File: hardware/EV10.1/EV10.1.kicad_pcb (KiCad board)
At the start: 4 copper layers, 72.7 x 89.4 mm, 122 parts, among them J1 Conn_01x02_Socket, J10 Conn_01x08_Socket, J11 Conn_01x06_Female, J13 Conn_01x04_Female, J2 Conn_01x02_Female, J5 Conn_01x02_Socket, J7 Conn_01x04_Female, J8 Conn_01x06_Female, SW4 SW_Push, SW5 SW_Push, U1 STM32F405RGTx, U11 ESP32-S3-WROOM-1-N8R2, U13 BM14B(0.8)-24DS-0.4V(53), U2 BQ21040DBVR, U3 CH340C, U5 STM32F030C8Tx, U6 WM8960CGEFL/RV, U7 TPS63060, Y1 Crystal_GND24

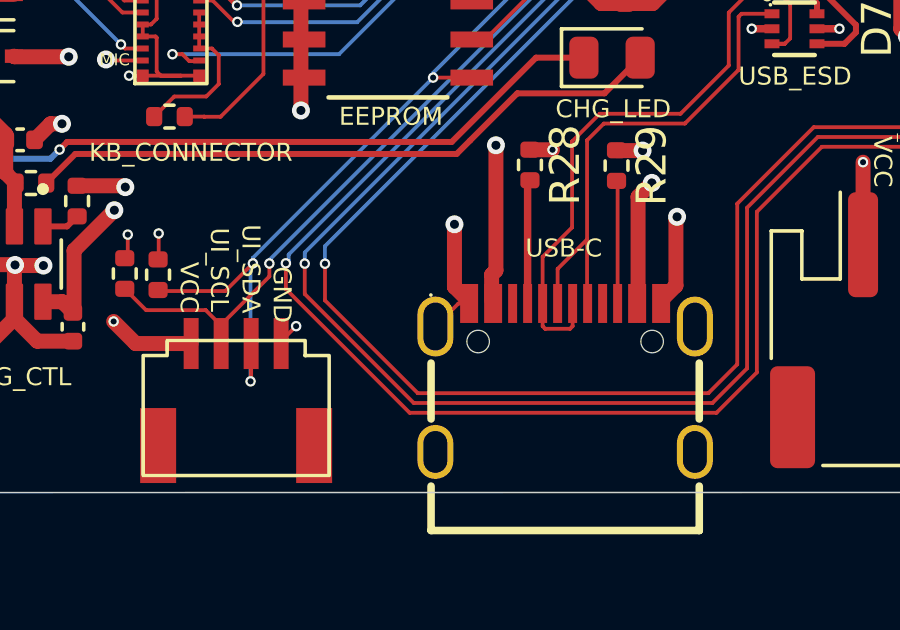
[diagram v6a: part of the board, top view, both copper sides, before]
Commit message: Fixed mistake that grounded the usb-c shield
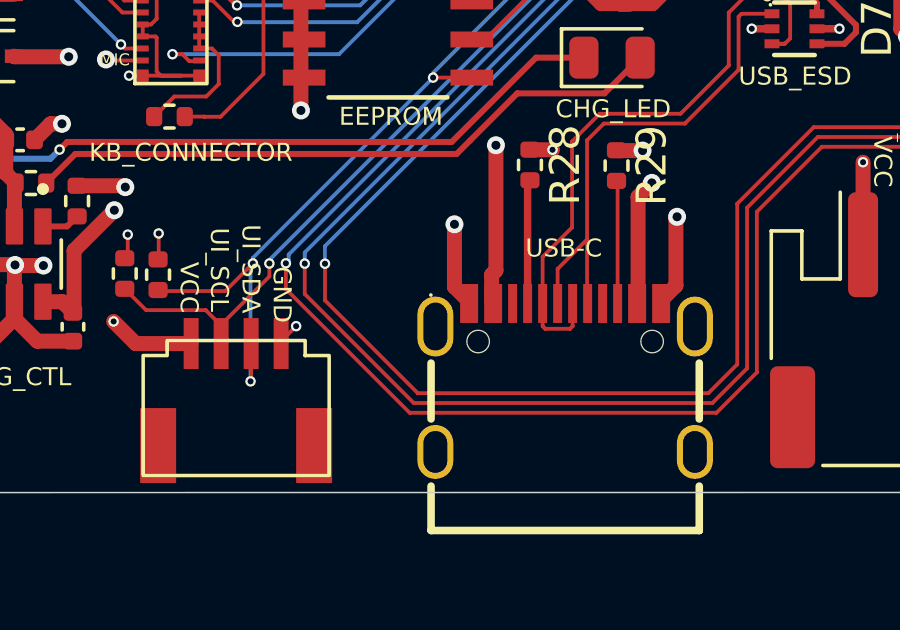
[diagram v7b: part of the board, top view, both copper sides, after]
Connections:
- USB-C1 pad 0: GND -> unconnected-(USB-C1-SH-Pad0)
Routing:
- net GND: track 573.6 -> 572.3 mm
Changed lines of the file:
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@@
 	(net 186 "Net-(U7-L1)")
 	(net 187 "Net-(U7-FB)")
+	(net 188 "unconnected-(USB-C1-SH-Pad0)")
 	(footprint "Capacitor_SMD:C_0805_2012Metric"
 		(layer "F.Cu")
@@
 			(layers "*.Cu" "*.Mask")
 			(remove_unused_layers no)
-			(net 4 "GND")
+			(net 188 "unconnected-(USB-C1-SH-Pad0)")
 			(pinfunction "SH")
-			(pintype "unspecified")
+			(pintype "unspecified+no_connect")
 		)
 		(pad "1" thru_hole oval
@@
 	)
 	(segment
-		(start 146.749544 139.133936)
-		(end 145.981192 139.902288)
-		(width 0.127)
-		(layer "F.Cu")
-		(net 4)
-	)
-	(segment
 		(start 181.452 77.18)
 		(end 181.48 77.208)
@@
 		(layer "F.Cu")
 		(net 4)
-	)
-	(segment
-		(start 146.9563 139.133936)
-		(end 146.749544 139.133936)
-		(width 0.127)
-		(layer "F.Cu")
-		(net 4)

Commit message: Added another test point to EV10.1 for BCLK. EV11 WIP
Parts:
- added TP13: P_I2S_BCLK, TestPoint:TestPoint_Keystone_5000-5004_Miniature, F.Cu at (148.0, 91.3)
- TP10: value P_UI_RX_NET -> P_UI_TX_NET
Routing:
- net /I2S_BCLK: track 27.8 -> 48.7 mm, vias 2 -> 3
